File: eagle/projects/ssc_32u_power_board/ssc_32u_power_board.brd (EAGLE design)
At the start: 167 x 106.5 mm, 36 parts, among them J1 691256610002, J10 ESQ-104-24-H-S, J11 ESQ-104-24-H-S, J12 ESQ-104-24-H-S, J13 ESQ-104-24-H-S, J14 MOL-SL-3-RA, J15 ESQ-103-24-H-S, J16 691256610002, J17 HMTSW-104-08-G-S-380, J18 HMTSW-104-08-G-S-380, J19 HMTSW-104-08-G-S-380, J2 HMTSW-104-08-G-S-380, J20 HMTSW-104-08-G-S-380, J21 ESQ-104-24-H-S, J22 ESQ-104-24-H-S, J23 ESQ-104-24-H-S, J24 ESQ-104-24-H-S, J25 ESQ-104-24-H-S, J26 ESQ-104-24-H-S, J27 ESQ-104-24-H-S, J28 ESQ-104-24-H-S, J3 HMTSW-104-08-G-S-380, J4 HMTSW-104-08-G-S-380, J5 HMTSW-104-08-G-S-380, J6 ESQ-104-24-H-S, J7 ESQ-104-24-H-S, J8 ESQ-104-24-H-S, J9 ESQ-104-24-H-S

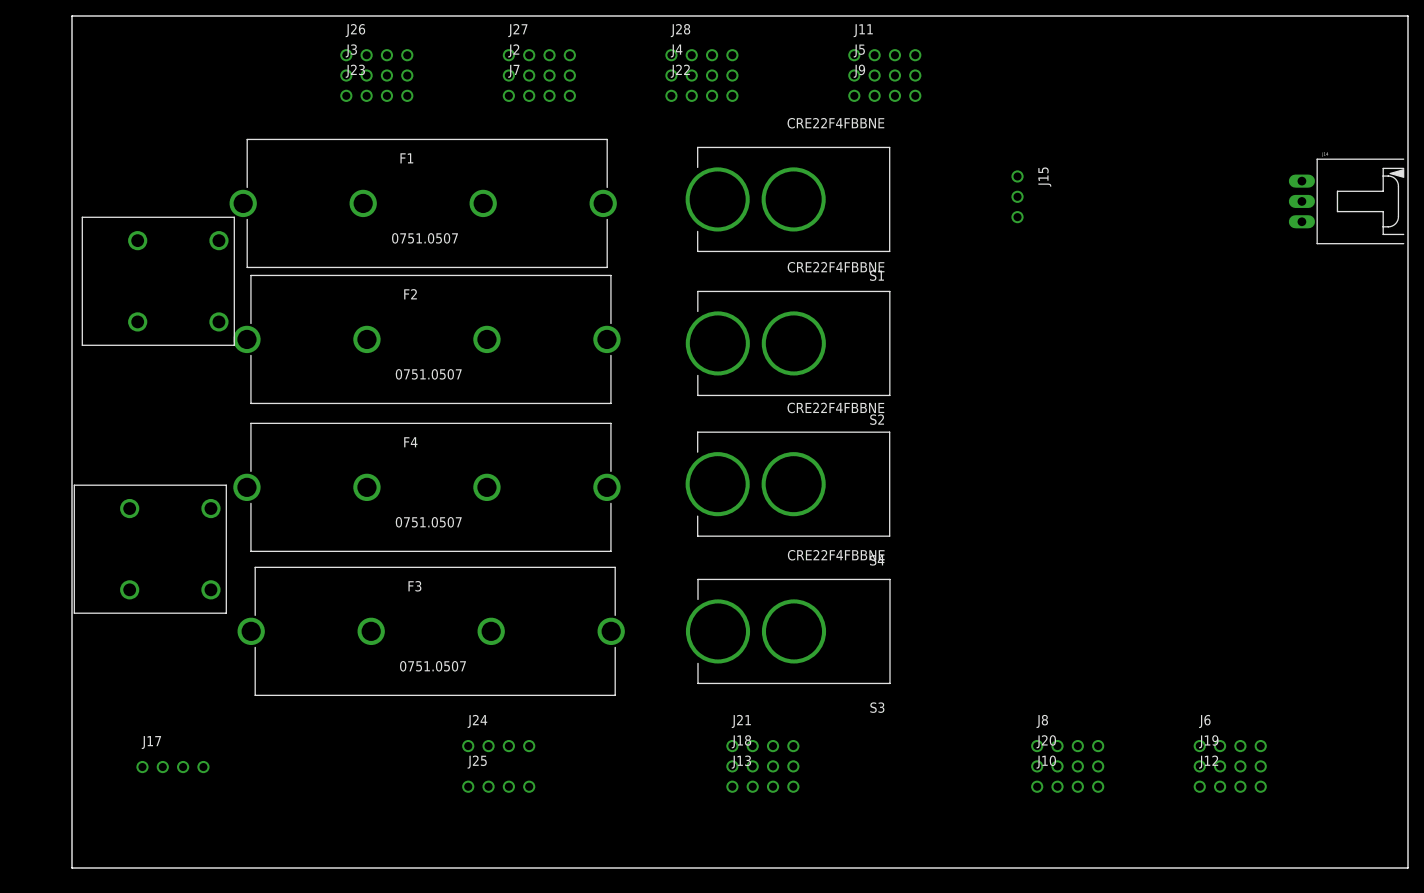
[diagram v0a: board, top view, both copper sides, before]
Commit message: Finished board layout, used polygons to fill all high current traces
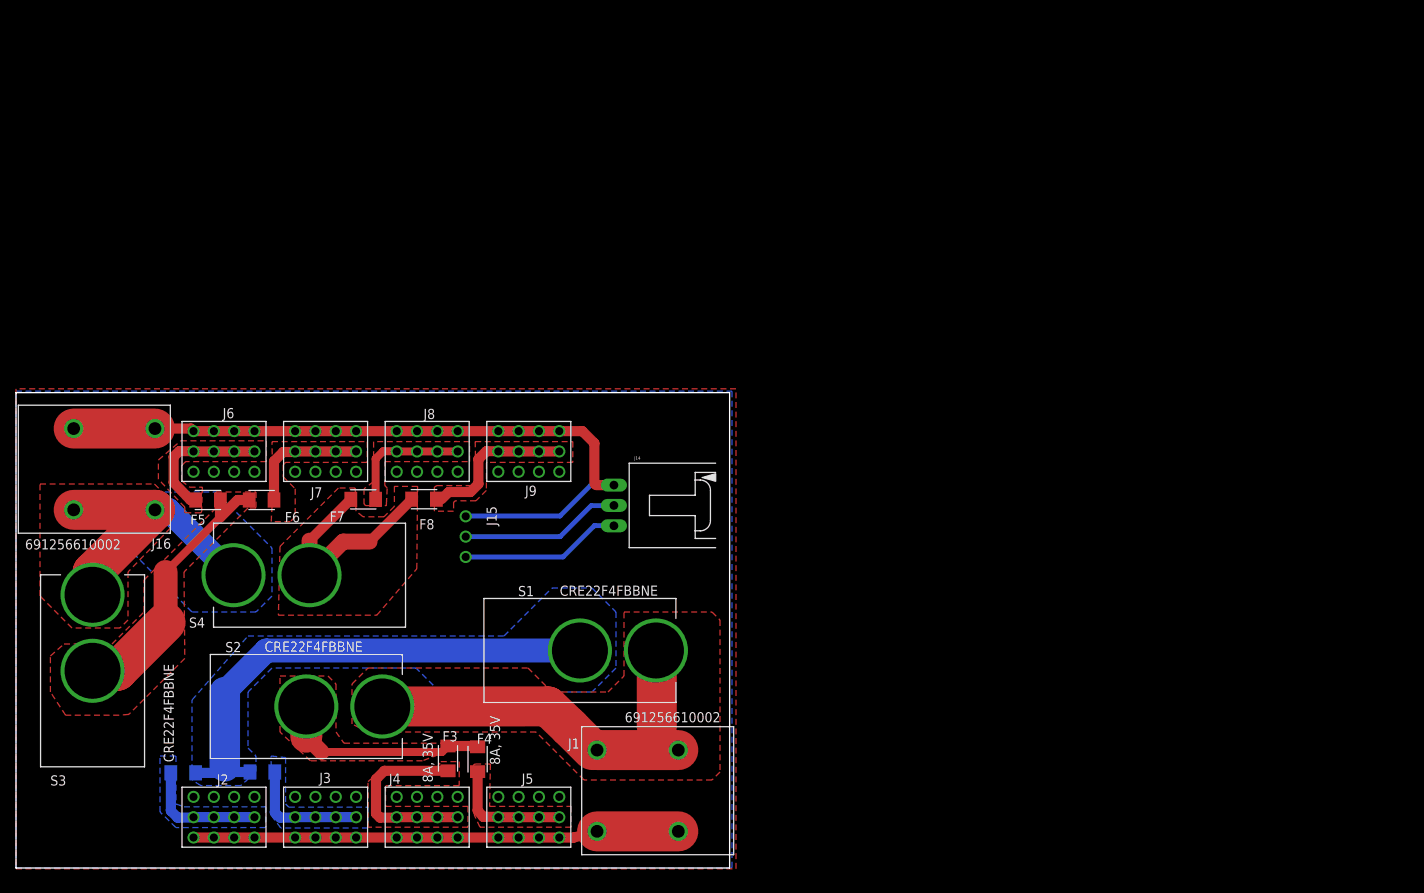
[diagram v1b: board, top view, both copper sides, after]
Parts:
- removed J10, J11, J12, J13, J21, J22, J23, J24, J25, J26, J27, J28: ESQ-104-24-H-S, ssc_32u_power_board:ESQ-104-24-H-S
- removed J17, J18, J19, J20: HMTSW-104-08-G-S-380, ssc_32u_power_board:HMTSW-104-08-G-S-380
- added F5, F6, F7, F8: 8A, 35V, ssc_32u_power_board:0437008.WR
- F1, F2, F3, F4: value 0751.0507 -> 8A, 35V; device ssc_32u_power_board:0751.0507 -> ssc_32u_power_board:0437008.WR
- J2, J3, J4, J5: value HMTSW-104-08-G-S-380 -> 4x3_2.54MM_HEADER; device ssc_32u_power_board:HMTSW-104-08-G-S-380 -> ssc_32u_power_board:2X_ESQ-104-24-H-S__HMTSW-104-08-G-S-380
- J6, J7, J8, J9: value ESQ-104-24-H-S -> 4x3_2.54MM_HEADER; device ssc_32u_power_board:ESQ-104-24-H-S -> ssc_32u_power_board:2X_ESQ-104-24-H-S__HMTSW-104-08-G-S-380
- moved J6 131.1 mm to (19.0, 52.1), turned to 180 degrees
- moved J5 102.8 mm to (57.1, 6.35)
- moved J2 100.7 mm to (19.0, 6.35)
- moved J4 98.9 mm to (44.4, 6.35)
- moved J14 94.0 mm to (75.4, 45.3)
- moved J3 92.9 mm to (31.7, 6.35)
- moved J8 88.1 mm to (44.4, 52.1), turned to 180 degrees
- moved S3 87.8 mm to (2.57, 24.6), turned to 90 degrees
- moved J1 85.7 mm to (70.7, 9.66), turned to 90 degrees
- moved J15 81.0 mm to (49.2, 41.4)
- moved F1 77.2 mm to (13.9, 11.9), flipped to the bottom, turned to 180 degrees
- moved S2 76.0 mm to (29.3, 20.2), turned to 0 degrees
- moved J9 62.9 mm to (57.1, 52.1), turned to 180 degrees
- moved S1 62.4 mm to (63.5, 27.2), turned to 0 degrees
- moved S4 61.6 mm to (29.7, 36.6)
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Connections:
- removed net BATT_1_FUSE_0_7: F1.P$3, F1.P$4, S1.P$1
- removed net BATT_1_FUSE_8_15: F2.P$3, F2.P$4, S2.P$1
- removed net BATT_1_SWITCH_0_7: J2.1, J2.2, J2.3, J2.4, J3.1, J3.2, J3.3, J3.4, S1.P$2
- removed net BATT_1_SWITCH_8_15: J4.1, J4.2, J4.3, J4.4, J5.1, J5.2, J5.3, J5.4, S2.P$2
- removed net BATT_2_FUSE_16_23: F3.P$3, F3.P$4, S3.P$1
- removed net BATT_2_FUSE_24_31: F4.P$3, F4.P$4, S4.P$1
- removed net BATT_2_SWITCH_16_23: J17.1, J17.2, J17.3, J17.4, J18.1, J18.2, J18.3, J18.4, S3.P$2
- removed net BATT_2_SWITCH_24_31: J19.1, J19.2, J19.3, J19.4, J20.1, J20.2, J20.3, J20.4, S4.P$2
- new net VBAT_1_FUSE_0_3: F1.P$2, J2.5, J2.6, J2.7, J2.8
- new net VBAT_1_FUSE_12_15: F4.P$2, J5.5, J5.6, J5.7, J5.8
- new net VBAT_1_FUSE_4_7: F2.P$2, J3.5, J3.6, J3.7, J3.8
- new net VBAT_1_FUSE_8_11: F3.P$2, J4.5, J4.6, J4.7, J4.8
- new net VBAT_1_SWITCH_0_7: F1.P$1, F2.P$1, S1.P$2
- new net VBAT_1_SWITCH_8_15: F3.P$1, F4.P$1, S2.P$2
- new net VBAT_2_FUSE_16_19: F5.P$2, J6.5, J6.6, J6.7, J6.8
- new net VBAT_2_FUSE_20_23: F6.P$2, J7.5, J7.6, J7.7, J7.8
- new net VBAT_2_FUSE_24_27: F7.P$2, J8.5, J8.6, J8.7, J8.8
- new net VBAT_2_FUSE_28_31: F8.P$2, J9.5, J9.6, J9.7, J9.8
- new net VBAT_2_SWITCH_16_23: F5.P$1, F6.P$1, S3.P$2
- new net VBAT_2_SWITCH_24_31: F7.P$1, F8.P$1, S4.P$2
- net BATT_1_VDD: now also S1.P$1, S2.P$1; no longer F1.P$1, F1.P$2, F2.P$1, F2.P$2
- net BATT_2_VDD: now also J16.P$3, J16.P$4, S3.P$1, S4.P$1; no longer F3.P$1, F3.P$2, F4.P$1, F4.P$2, J16.P$1, J16.P$2
- net GND: now also J16.P$1, J16.P$2, J2.10, J2.11, J2.12, J2.9, J3.10, J3.11, J3.12, J3.9, J4.10, J4.11, J4.12, J4.9, J5.10, J5.11, J5.12, J5.9, J6.10, J6.11, J6.12, J6.9, J7.10, J7.11, J7.12, J7.9, J8.10, J8.11, J8.12, J8.9, J9.10, J9.11, J9.12, J9.9; no longer J10.1, J10.2, J10.3, J10.4, J11.1, J11.2, J11.3, J11.4, J12.1, J12.2, J12.3, J12.4, J13.1, J13.2, J13.3, J13.4, J16.P$3, J16.P$4, J25.1, J25.2, J25.3, J25.4, J26.1, J26.2, J26.3, J26.4, J27.1, J27.2, J27.3, J27.4, J28.1, J28.2, J28.3, J28.4
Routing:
- net GND: track 0.00 -> 154.3 mm
- net VBAT_1_SWITCH_0_7: track 0.00 -> 63.3 mm
- net BATT_1_VDD: track 0.00 -> 52.8 mm
- net BATT_2_VDD: track 0.00 -> 37.2 mm
- net VBAT_2_SWITCH_16_23: track 0.00 -> 34.3 mm
- net VBAT_2_SWITCH_24_31: track 0.00 -> 28.3 mm
- net VBAT_1_SWITCH_8_15: track 0.00 -> 26.4 mm
- net VBAT_1_FUSE_8_11: track 0.00 -> 24.2 mm
- net BBB_RX_SSC_TX: track 0.00 -> 20.2 mm
- net BBB_TX_SSC_RX: track 0.00 -> 20.1 mm
- net VBAT_2_FUSE_28_31: track 0.00 -> 19.7 mm
- net VBAT_2_FUSE_16_19: track 0.00 -> 17.3 mm
- net VBAT_2_FUSE_24_27: track 0.00 -> 15.7 mm
- net VBAT_2_FUSE_20_23: track 0.00 -> 15.6 mm
- net VBAT_1_FUSE_0_3: track 0.00 -> 15.6 mm
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- added copper zone on layer 1, net BATT_1_VDD
- added copper zone on layer 1, net BATT_2_VDD
- added copper zone on layer 16, net BATT_2_VDD
- added copper zone on layer 1, net GND
- added copper zone on layer 16, net GND
- added copper zone on layer 16, net VBAT_1_FUSE_0_3
- added copper zone on layer 1, net VBAT_1_FUSE_12_15
- added copper zone on layer 16, net VBAT_1_FUSE_4_7
- added copper zone on layer 1, net VBAT_1_FUSE_8_11
- added copper zone on layer 16, net VBAT_1_SWITCH_0_7
- added copper zone on layer 1, net VBAT_1_SWITCH_8_15
- added copper zone on layer 1, net VBAT_2_FUSE_16_19
- added copper zone on layer 1, net VBAT_2_FUSE_20_23
- added copper zone on layer 1, net VBAT_2_FUSE_24_27
- added copper zone on layer 1, net VBAT_2_FUSE_28_31
- added copper zone on layer 1, net VBAT_2_SWITCH_16_23
- added copper zone on layer 1, net VBAT_2_SWITCH_24_31
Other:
- board size 167 x 106.5 mm -> 89.2 x 59.4 mm

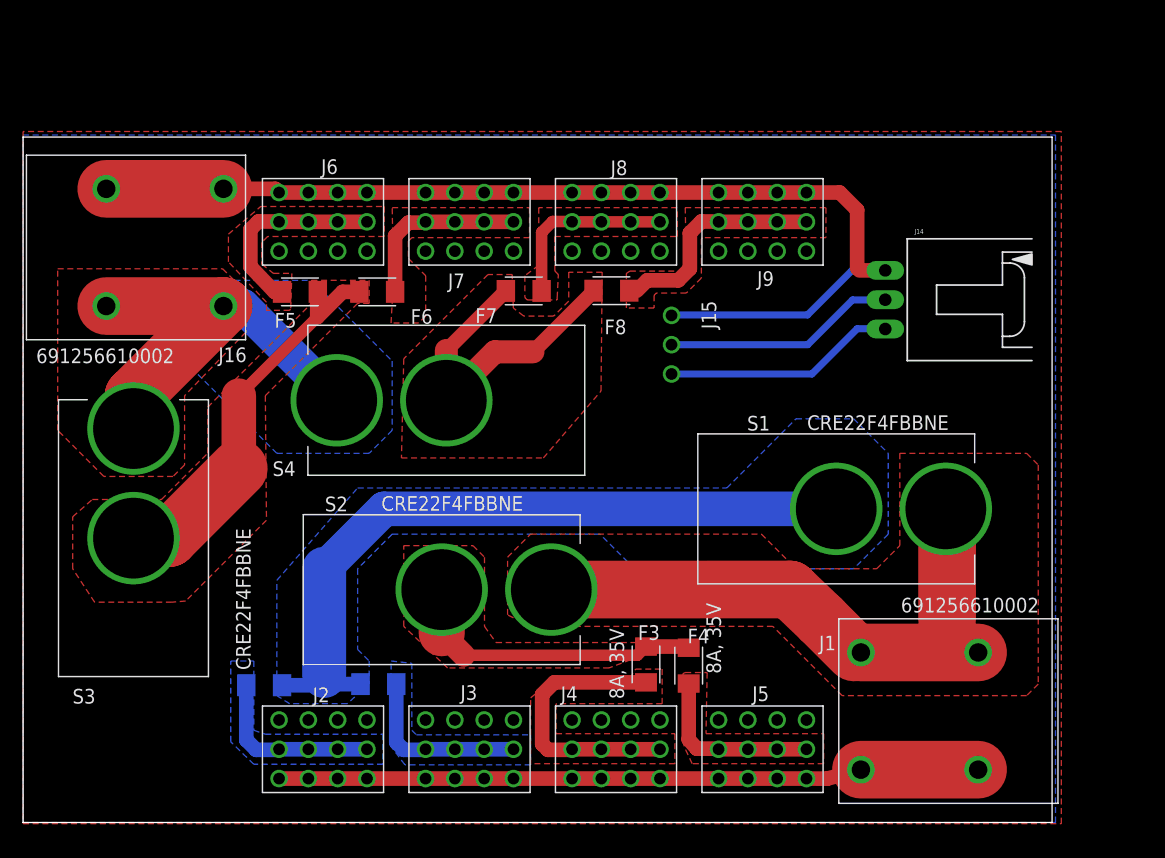
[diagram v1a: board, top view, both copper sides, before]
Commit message: Major modifications, removed switches and swapped out surface mount fuses for glass ones. Still two layer board
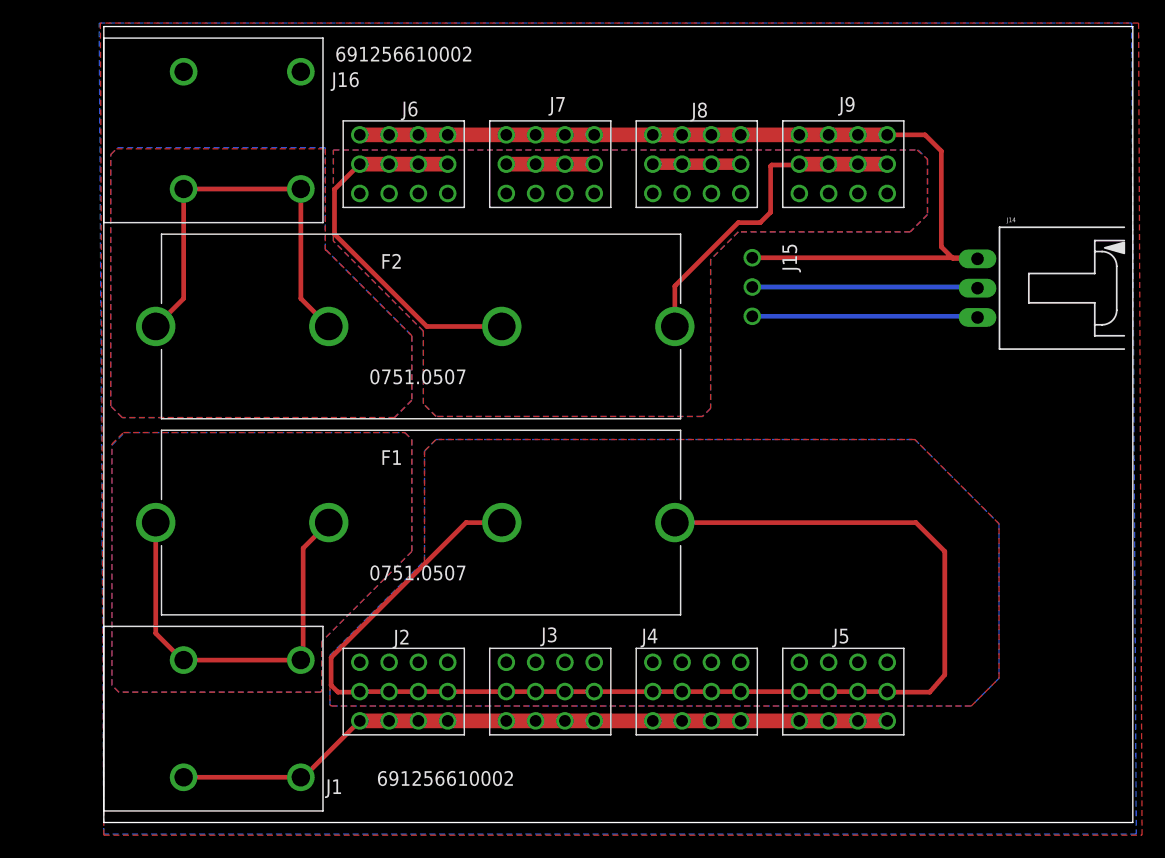
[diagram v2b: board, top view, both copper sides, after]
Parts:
- removed F3, F4, F5, F6, F7, F8: 8A, 35V, ssc_32u_power_board:0437008.WR
- removed S1, S2, S3, S4: CRE22F4FBBNE, ssc_32u_power_board:CRE22F4FBBNE
- F1, F2: value 8A, 35V -> 0751.0507; device ssc_32u_power_board:0437008.WR -> ssc_32u_power_board:0751.0507
- moved J1 58.7 mm to (12.0, 9.00), turned to 270 degrees
- moved F2 31.2 mm to (27.0, 43.0), flipped to the top
- moved F1 19.2 mm to (27.0, 26.0), flipped to the top, turned to 0 degrees
- moved J16 12.2 mm to (12.0, 60.0)
- moved J3 8.60 mm to (38.7, 11.3)
- moved J7 8.60 mm to (38.7, 57.1)
- moved J15 8.60 mm to (56.2, 46.4)
- moved J2 8.60 mm to (26.0, 11.3)
- moved J4 8.60 mm to (51.4, 11.3)
- moved J6 8.60 mm to (26.0, 57.1)
- moved J8 8.60 mm to (51.4, 57.1)
- moved J5 8.60 mm to (64.1, 11.3)
- moved J9 8.60 mm to (64.1, 57.1)
- moved J14 8.06 mm to (83.4, 46.3)
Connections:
- removed net VBAT_1_FUSE_0_3: F1.P$2, J2.5, J2.6, J2.7, J2.8
- removed net VBAT_1_FUSE_12_15: F4.P$2, J5.5, J5.6, J5.7, J5.8
- removed net VBAT_1_FUSE_4_7: F2.P$2, J3.5, J3.6, J3.7, J3.8
- removed net VBAT_1_FUSE_8_11: F3.P$2, J4.5, J4.6, J4.7, J4.8
- removed net VBAT_1_SWITCH_0_7: F1.P$1, F2.P$1, S1.P$2
- removed net VBAT_1_SWITCH_8_15: F3.P$1, F4.P$1, S2.P$2
- removed net VBAT_2_FUSE_16_19: F5.P$2, J6.5, J6.6, J6.7, J6.8
- removed net VBAT_2_FUSE_20_23: F6.P$2, J7.5, J7.6, J7.7, J7.8
- removed net VBAT_2_FUSE_24_27: F7.P$2, J8.5, J8.6, J8.7, J8.8
- removed net VBAT_2_FUSE_28_31: F8.P$2, J9.5, J9.6, J9.7, J9.8
- removed net VBAT_2_SWITCH_16_23: F5.P$1, F6.P$1, S3.P$2
- removed net VBAT_2_SWITCH_24_31: F7.P$1, F8.P$1, S4.P$2
- new net VBAT_1_FUSE_0_15: F1.P$3, F1.P$4, J2.5, J2.6, J2.7, J2.8, J3.5, J3.6, J3.7, J3.8, J4.5, J4.6, J4.7, J4.8, J5.5, J5.6, J5.7, J5.8
- new net VBAT_2_FUSE_16_24_31: F2.P$3, F2.P$4, J6.5, J6.6, J6.7, J6.8, J7.5, J7.6, J7.7, J7.8, J8.5, J8.6, J8.7, J8.8, J9.5, J9.6, J9.7, J9.8
- net BATT_1_VDD: now also F1.P$1, F1.P$2, J1.P$1, J1.P$2; no longer J1.P$3, J1.P$4, S1.P$1, S2.P$1
- net BATT_2_VDD: now also F2.P$1, F2.P$2; no longer S3.P$1, S4.P$1
- net GND: now also J1.P$3, J1.P$4; no longer J1.P$1, J1.P$2
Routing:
- net VBAT_1_FUSE_0_15: track 0.00 -> 111.3 mm
- net VBAT_2_FUSE_16_24_31: track 0.00 -> 76.3 mm
- net VBAT_1_SWITCH_0_7: track 63.3 -> 0.00 mm
- net VBAT_2_SWITCH_16_23: track 34.3 -> 0.00 mm
- net VBAT_2_SWITCH_24_31: track 28.3 -> 0.00 mm
- net VBAT_1_SWITCH_8_15: track 26.4 -> 0.00 mm
- net VBAT_1_FUSE_8_11: track 24.2 -> 0.00 mm
- net VBAT_2_FUSE_28_31: track 19.7 -> 0.00 mm
- net VBAT_2_FUSE_16_19: track 17.3 -> 0.00 mm
- net BATT_1_VDD: track 52.8 -> 36.3 mm
- net VBAT_2_FUSE_24_27: track 15.7 -> 0.00 mm
- net VBAT_2_FUSE_20_23: track 15.6 -> 0.00 mm
- net VBAT_1_FUSE_0_3: track 15.6 -> 0.00 mm
- net VBAT_1_FUSE_4_7: track 15.5 -> 0.00 mm
- net VBAT_1_FUSE_12_15: track 15.4 -> 0.00 mm
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- added copper zone on layer 16, net BATT_1_VDD
- added copper zone on layer 1, net VBAT_1_FUSE_0_15
- added copper zone on layer 16, net VBAT_1_FUSE_0_15
- added copper zone on layer 1, net VBAT_2_FUSE_16_24_31
- added copper zone on layer 16, net VBAT_2_FUSE_16_24_31
- removed copper zone on layer 16, net VBAT_1_FUSE_0_3
- removed copper zone on layer 1, net VBAT_1_FUSE_12_15
- removed copper zone on layer 16, net VBAT_1_FUSE_4_7
- removed copper zone on layer 1, net VBAT_1_FUSE_8_11
- removed copper zone on layer 16, net VBAT_1_SWITCH_0_7
- removed copper zone on layer 1, net VBAT_1_SWITCH_8_15
- removed copper zone on layer 1, net VBAT_2_FUSE_16_19
- removed copper zone on layer 1, net VBAT_2_FUSE_20_23
- removed copper zone on layer 1, net VBAT_2_FUSE_24_27
- removed copper zone on layer 1, net VBAT_2_FUSE_28_31
- removed copper zone on layer 1, net VBAT_2_SWITCH_16_23
- removed copper zone on layer 1, net VBAT_2_SWITCH_24_31
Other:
- board size 89.2 x 59.4 mm -> 89.2 x 69 mm
